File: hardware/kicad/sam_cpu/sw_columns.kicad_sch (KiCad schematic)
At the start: 35 parts, among them J1 J1 SWITCH COLUMNS, Q11 MMBT3904, Q12 MMBT3904, Q13 MMBT3904, Q14 MMBT3904, Q15 MMBT3904, Q16 MMBT3904, Q17 MMBT3904, Q18 MMBT3904, U20 74HC595

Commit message: Use 3.96 mm KK-396 footprints for the switch harness connectors
J1, J2, J3, J6, J12 and J13 are 0.156" headers on the original board, so
the existing harness plugs need KK-396, as already used for J10 and J11.

Co-Authored-By: Claude Opus 5.5 (1M context) <noreply@anthropic.com>
Claude-Session: https://claude.ai/code/session_019DLTv1F2PjepjxqiUcAMKV
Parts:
- J1: footprint Connector_Molex:Molex_KK-254_AE-6410-09A_1x09_P2.54mm_Vertical -> Connector_Molex:Molex_KK-396_A-41791-0009_1x09_P3.96mm_Vertical
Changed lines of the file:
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@@
 			)
 		)
-		(property "Footprint" "Connector_Molex:Molex_KK-254_AE-6410-09A_1x09_P2.54mm_Vertical"
+		(property "Footprint" "Connector_Molex:Molex_KK-396_A-41791-0009_1x09_P3.96mm_Vertical"
 			(at 233.68 152.4 0)
 			(hide yes)

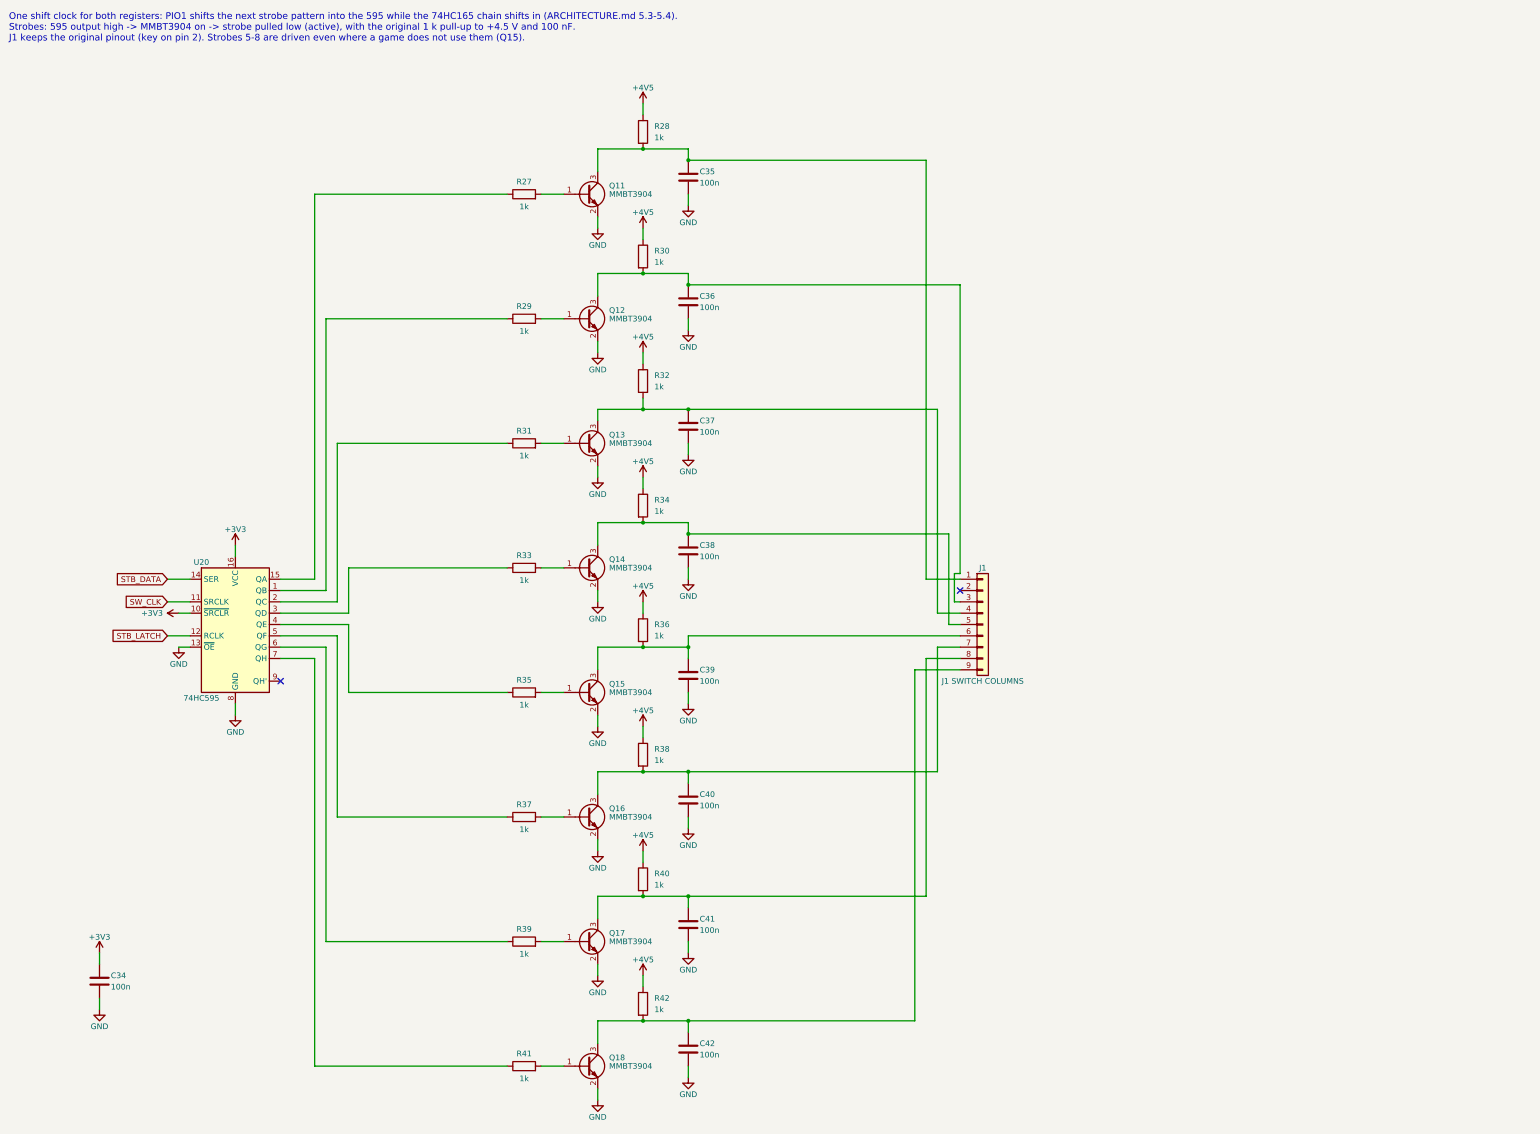
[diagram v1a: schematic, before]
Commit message: Add RTC, test points and stereo speaker connector; place all parts on 2 layers
Schematic: DS3231MZ real-time clock on the Pi I2C1 with a CR2032 holder,
22 test points (rails, bus, strobes, switch chain, VREF, DAC outputs) and
J22, a second KK-396 speaker connector with L and R as separate pairs.
ERC 0 errors, generated netlist matches the intended nets.

PCB: 2 copper layers. The RP2354B sits near J9 with its USB-C on the top
edge 13 mm from the USB pins; decoupling, regulator and crystal parts on
their pins; every other part grouped by sheet next to its connector, low
parts only under the Pi. J17 and J22 on the right edge; Pi and J5 12 mm
lower to fit the audio parts.

Co-Authored-By: Claude Opus 5.5 (1M context) <noreply@anthropic.com>
Claude-Session: https://claude.ai/code/session_01ExuDVoDDDHhVWjb8EwVzYb
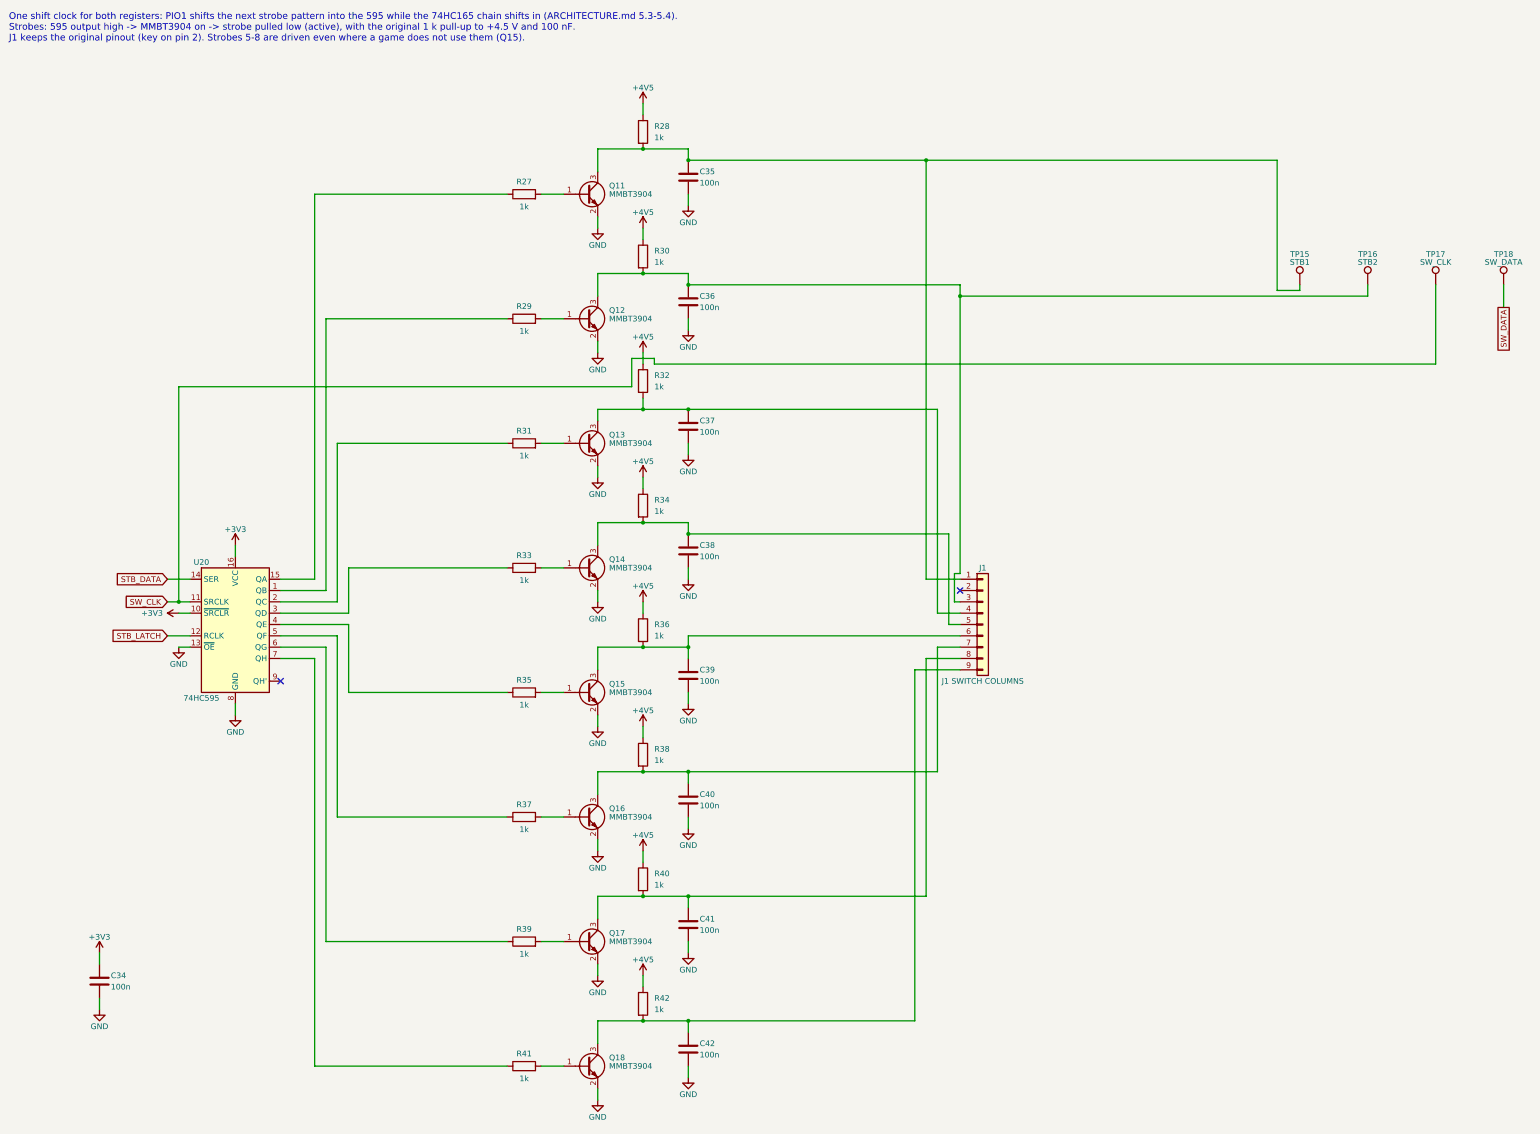
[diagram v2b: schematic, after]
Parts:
- added TP15: STB1, TestPoint:TestPoint_Pad_D1.5mm, symbol Connector:TestPoint
- added TP16: STB2, TestPoint:TestPoint_Pad_D1.5mm, symbol Connector:TestPoint
- added TP17: SW_CLK, TestPoint:TestPoint_Pad_D1.5mm, symbol Connector:TestPoint
- added TP18: SW_DATA, TestPoint:TestPoint_Pad_D1.5mm, symbol Connector:TestPoint
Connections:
- net SW_CLK: now also TP17.1
- net at C36.1, J1.3 (Pin_3), Q12.3 (C)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: now also TP16.1
- net at C35.1, J1.1 (Pin_1), Q11.3 (C)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: now also TP15.1
- new net SW_DATA: TP18.1

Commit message: Audio on external 12 V with TDA7297 stereo + subwoofer amps, NCP1117, guide regulator layout
- Remove the +-12 V input from J11; J23 external +12 V with polyfuse and TVS
- Replace the two TDA2030A with a TDA7297 bridge amp for left/right (J10, J22)
  and a second TDA7297 for the subwoofer (J24), fed by an (L+R)/2 110 Hz
  Sallen-Key low-pass (OPA1678); shared standby and RP2354B-controlled mute
- AMS1117 -> NCP1117-3.3 (ceramic-stable, as in the RP2350 guide), 10 uF 1206
- L1 and crystal part numbers from the RP2350 hardware guide
- Place the core regulator parts by hand following the Pico 2 layout; amps in a
  row with a heatsink keep-out; J23/J22/J24 on the right edge

Co-Authored-By: Claude Opus 5.5 (1M context) <noreply@anthropic.com>
Claude-Session: https://claude.ai/code/session_01ExuDVoDDDHhVWjb8EwVzYb
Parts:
- removed TP18: SW_DATA, TestPoint:TestPoint_Pad_D1.5mm, symbol Connector:TestPoint
- added TP14: STB1, TestPoint:TestPoint_Pad_D1.5mm, symbol Connector:TestPoint
- TP15: value STB1 -> STB2
- TP16: value STB2 -> SW_CLK
- TP17: value SW_CLK -> SW_DATA
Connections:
- net SW_CLK: now also TP16.1; no longer TP17.1
- net SW_DATA: now also TP17.1
- net at C36.1, J1.3 (Pin_3), Q12.3 (C)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: now also TP15.1; no longer TP16.1
- net at C35.1, J1.1 (Pin_1), Q11.3 (C)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: now also TP14.1; no longer TP15.1
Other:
- moved on the sheet: TP15, TP16, TP17

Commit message: Add two HD DMD panels on a PIO parallel bus (incremental edit)
RP2354B GPIO20-36 drive two HUB75 panels (J25/J26) through 3 x 74AHCT245
with shared CLK/LAT/OE and A/B row lines; J5 shares DMD_D0-D6. The 165
load and 595 latch share GPIO17; coin door moves to a 7th 165 (U30),
LED_STATUS and GI_SPARE to a new first 595 (U31). Board widened to 142 mm
below the Pi. Sheets and board edited in place via tools/changes, no
existing footprint moved.

Co-Authored-By: Claude Opus 5.5 (1M context) <noreply@anthropic.com>
Claude-Session: https://claude.ai/code/session_01ExuDVoDDDHhVWjb8EwVzYb
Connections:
- net STB_DATA renamed STB_CHAIN
- net STB_LATCH renamed SW_LOAD_N
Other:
- note added: "U20 latch shares SW_LOAD_N with the 74HC165 load (one pulse: 165 loads while low, 595 latches on the rising edge). U20 now follows U31 (DMD panels sheet), which carries the status LED and GI_SPARE. One shift clock for both registers: PIO1 shifts the next strobe pattern into the 595 while the 74HC165 chain shifts in (ARCHITECTURE.md 5.3-5.4). Strobes: 595 output high -> MMBT3904 on -> strobe pulle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"
- note removed: "One shift clock for both registers: PIO1 shifts the next strobe pattern into the 595 while the 74HC165 chain shifts in (ARCHITECTURE.md 5.3-5.4). Strobes: 595 output high -> MMBT3904 on -> strobe pulled low (active), with the original 1 k pull-up to +4.5 V and 100 nF. J1 keeps the original pinout (key on pin 2). Strobes 5-8 are driven even where a game does not use them (Q15)."
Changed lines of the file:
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@@
 		(company "Stern SAM CPU PPUC (CERN-OHL-S v2)")
 	)
-	(text "One shift clock for both registers: PIO1 shifts the next strobe pattern into the 595 while the 74HC165 chain shifts in (ARCHITECTURE.md 5.3-5.4).\nStrobes: 595 output high -> MMBT3904 on -> strobe pulled low (active), with the original 1 k pull-up to +4.5 V and 100 nF.\nJ1 keeps the original pinout (key on pin 2). Strobes 5-8 are driven even where a game does not use them (Q15)."
+	(text "U20 latch shares SW_LOAD_N with the 74HC165 load (one pulse: 165 loads while low, 595 latches on the rising edge). U20 now follows U31 (DMD panels sheet), which carries the status LED and GI_SPARE.\nOne shift clock for both registers: PIO1 shifts the next strobe pattern into the 595 while the 74HC165 chain shifts in (ARCHITECTURE.md 5.3-5.4).\nStrobes: 595 output high -> MMBT3904 on -> strobe pulled low (active), with the original 1 k pull-up to +4.5 V and 100 nF.\nJ1 keeps the original pinout (key on pin 2). Strobes 5-8 are driven even where a game does not use them (Q15)."
 		(exclude_from_sim no)
 		(at 15.24 15.24 0)
@@
 		)
 	)
-	(global_label "STB_LATCH"
+	(global_label "SW_LOAD_N"
 		(shape input)
 		(at 50.8 154.94 180)
@@
 		)
 	)
-	(global_label "STB_DATA"
+	(global_label "STB_CHAIN"
 		(shape input)
 		(at 50.8 142.24 180)

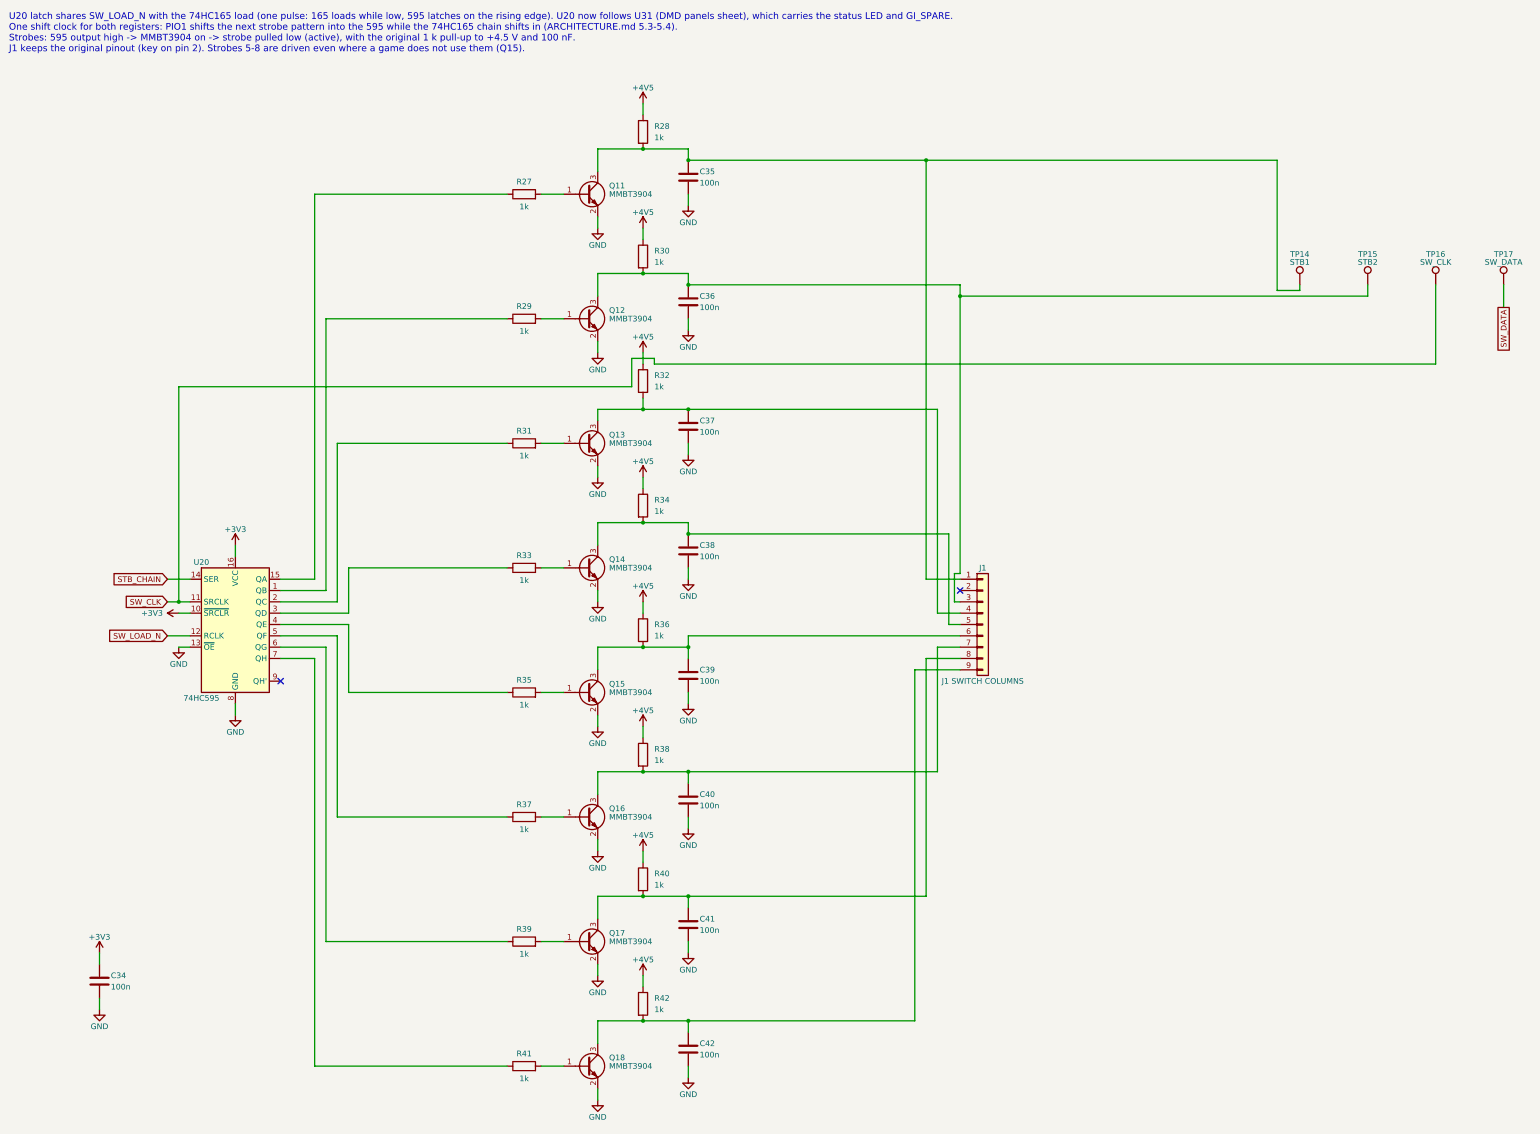
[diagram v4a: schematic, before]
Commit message: DIP switch block not loaded; larger schematic text
c30: SW3, R168-R175, U14 and C93 flagged DNP (schematic and board).
c31: schematic text 1.27 -> 1.6 mm (pins 1.5 mm), intersheet refs moved out.

Co-Authored-By: Claude Opus 5.5 (1M context) <noreply@anthropic.com>
Claude-Session: https://claude.ai/code/session_01ExuDVoDDDHhVWjb8EwVzYb
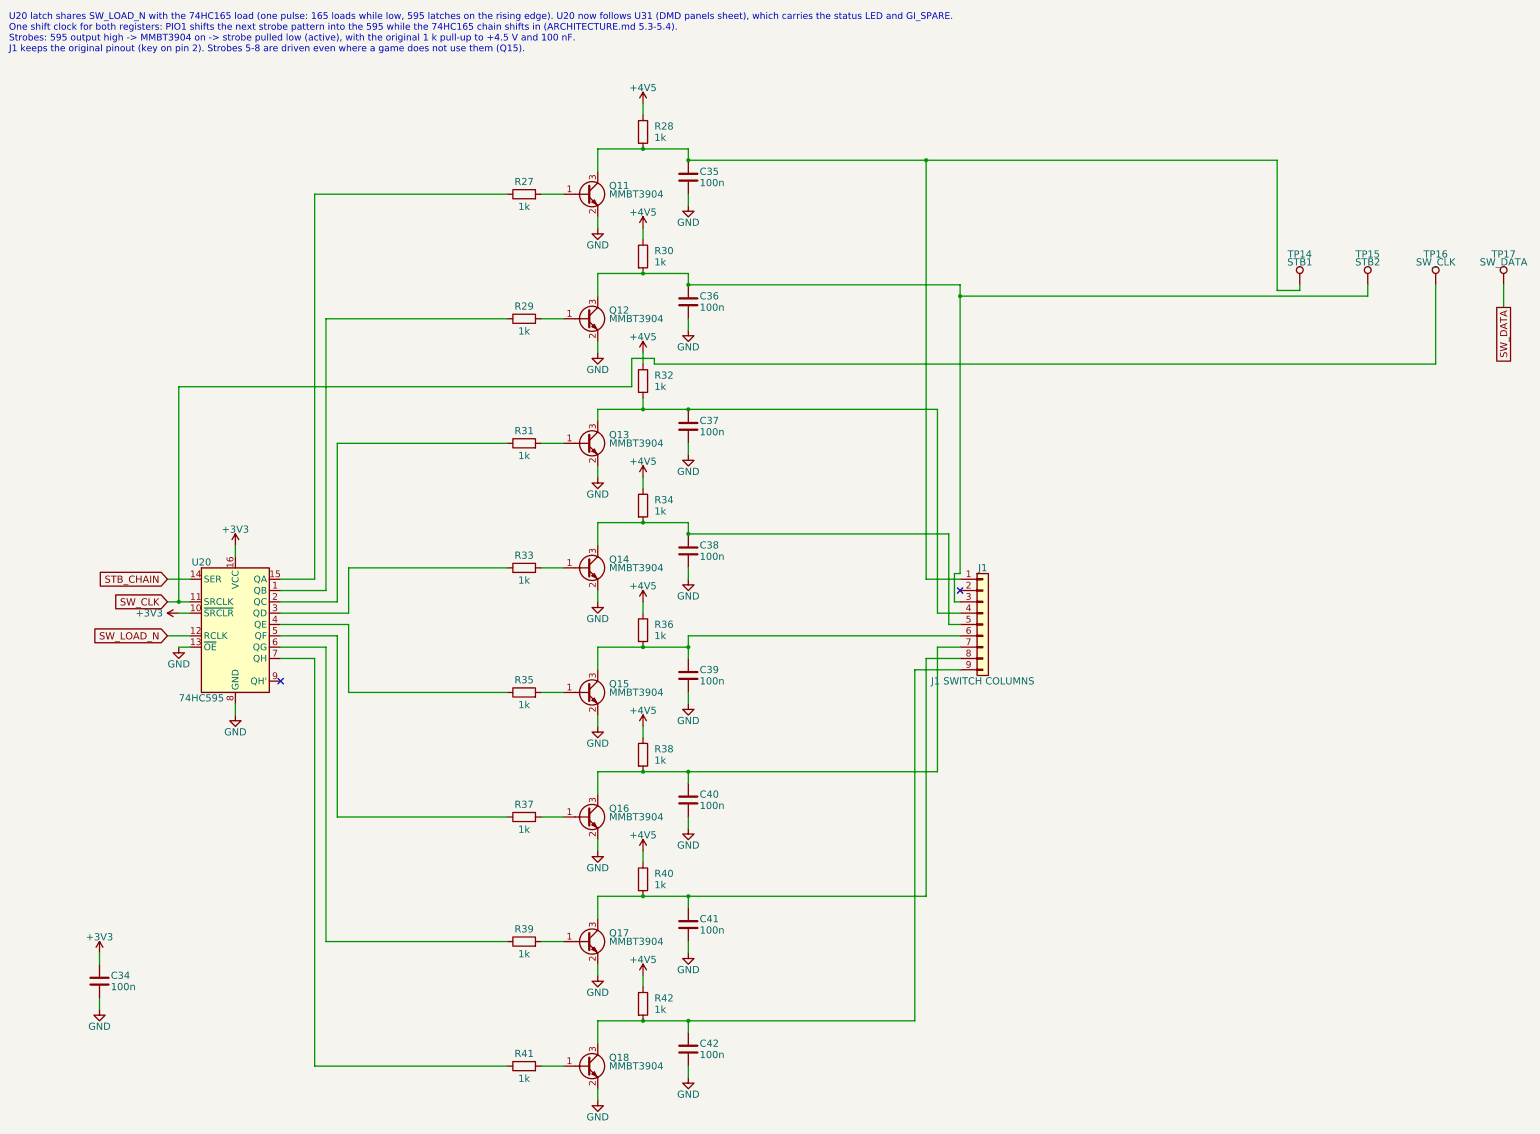
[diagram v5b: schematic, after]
